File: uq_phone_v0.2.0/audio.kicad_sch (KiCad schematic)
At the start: 31 parts, among them J1 PJ-605-6A, U13 TS3A5018RSVR, U14 NAU88C22YG, U9 AZV5001RA4-7

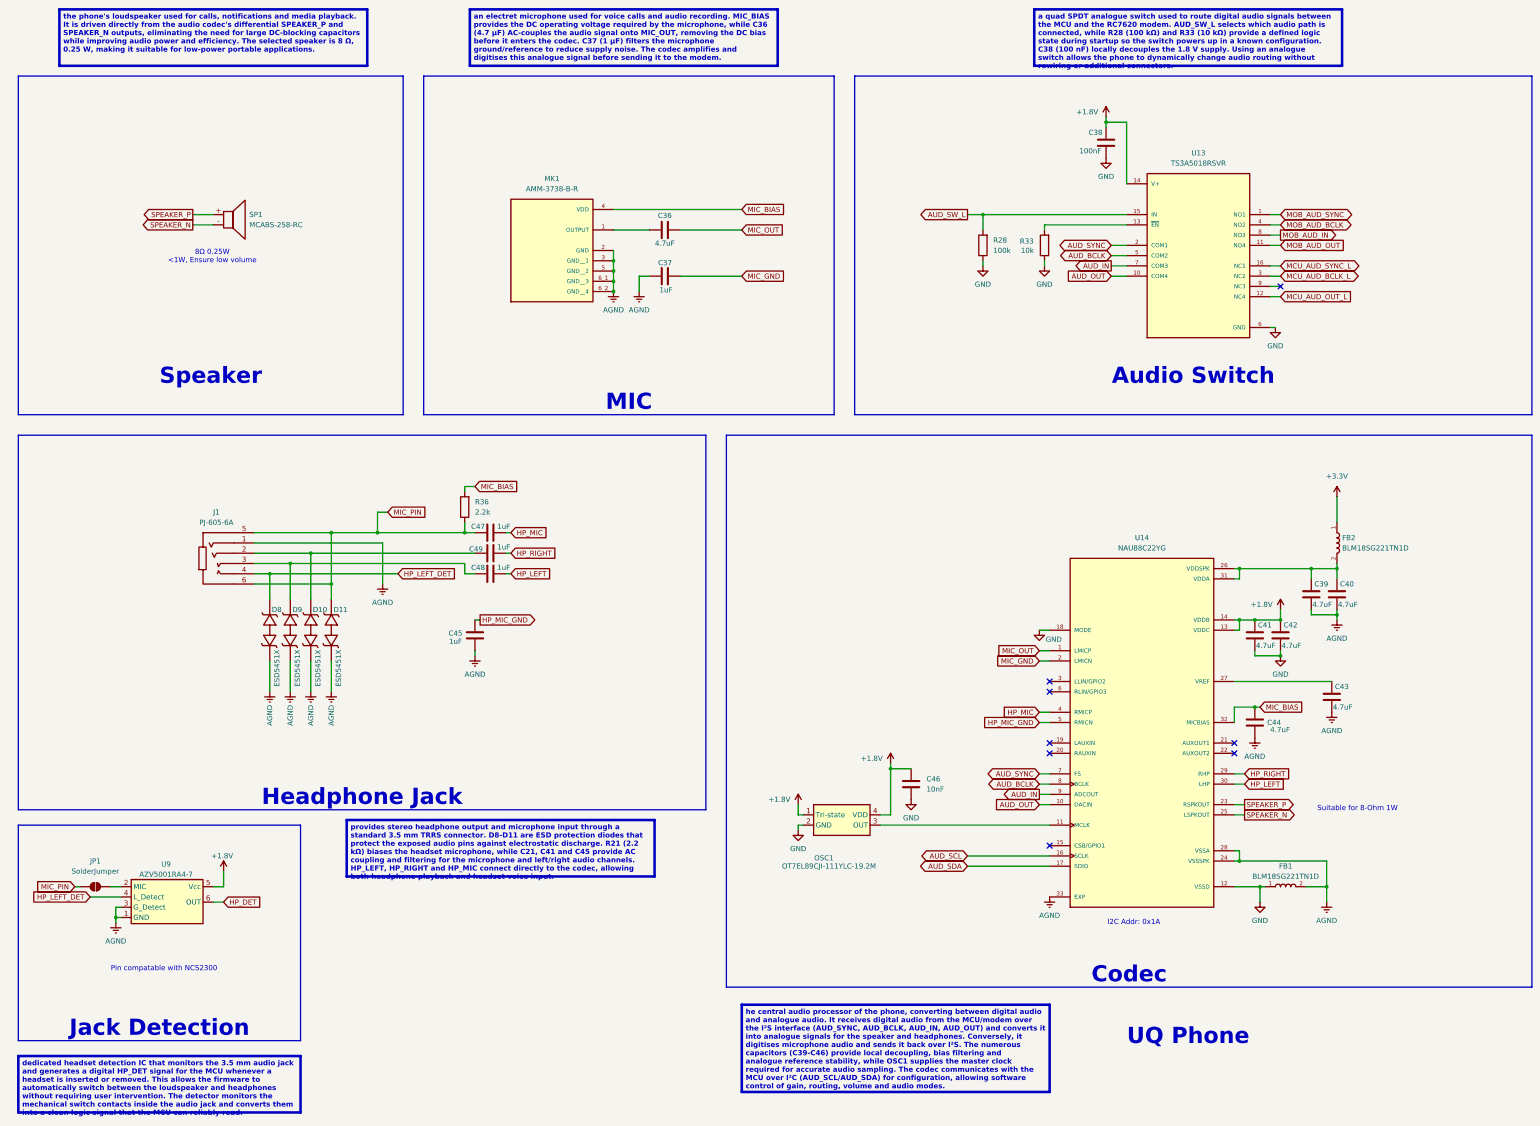
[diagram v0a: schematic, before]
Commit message: Add headphone breakout board and update main PCB
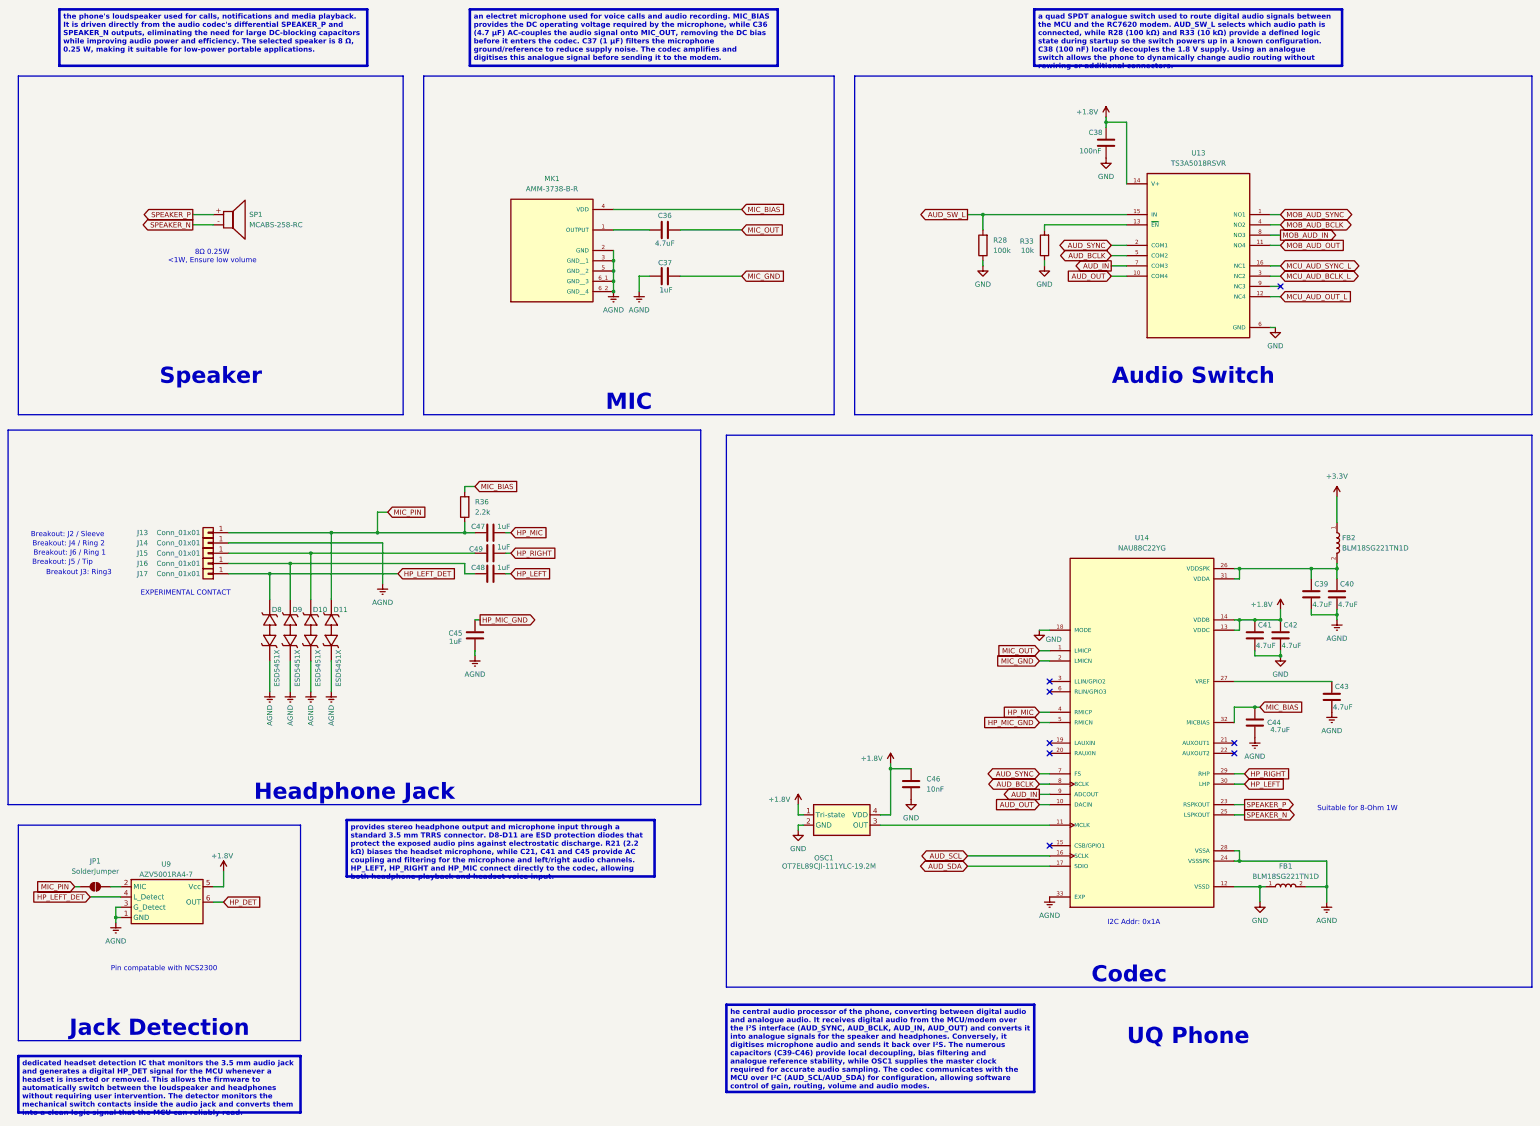
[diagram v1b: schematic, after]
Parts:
- removed J1: PJ-605-6A, custom_footprints:AUDIO-TH_PJ-605-6A, symbol Misc:PJ-605-6A
- added J13, J14, J15, J16, J17: Conn_01x01, headphone_board:Breakout_Mating_Pad, symbol Connector_Generic:Conn_01x01
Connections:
- net AGND: now also J14.1 (Pin_1)
- net HP_LEFT_DET: now also J17.1 (Pin_1)
- net MIC_PIN: now also J13.1 (Pin_1)
- net at C48.2, D9.2: now also J16.1 (Pin_1)
- net at C49.2, D10.2: now also J15.1 (Pin_1)
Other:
- note added: "Breakout J3: Ring3"
- note added: "Breakout: J2 / Sleeve"
- note added: "Breakout: J4 / Ring 2"
- note added: "Breakout: J5 / Tip"
- note added: "Breakout: J6 / Ring 1"
- note added: "EXPERIMENTAL CONTACT"

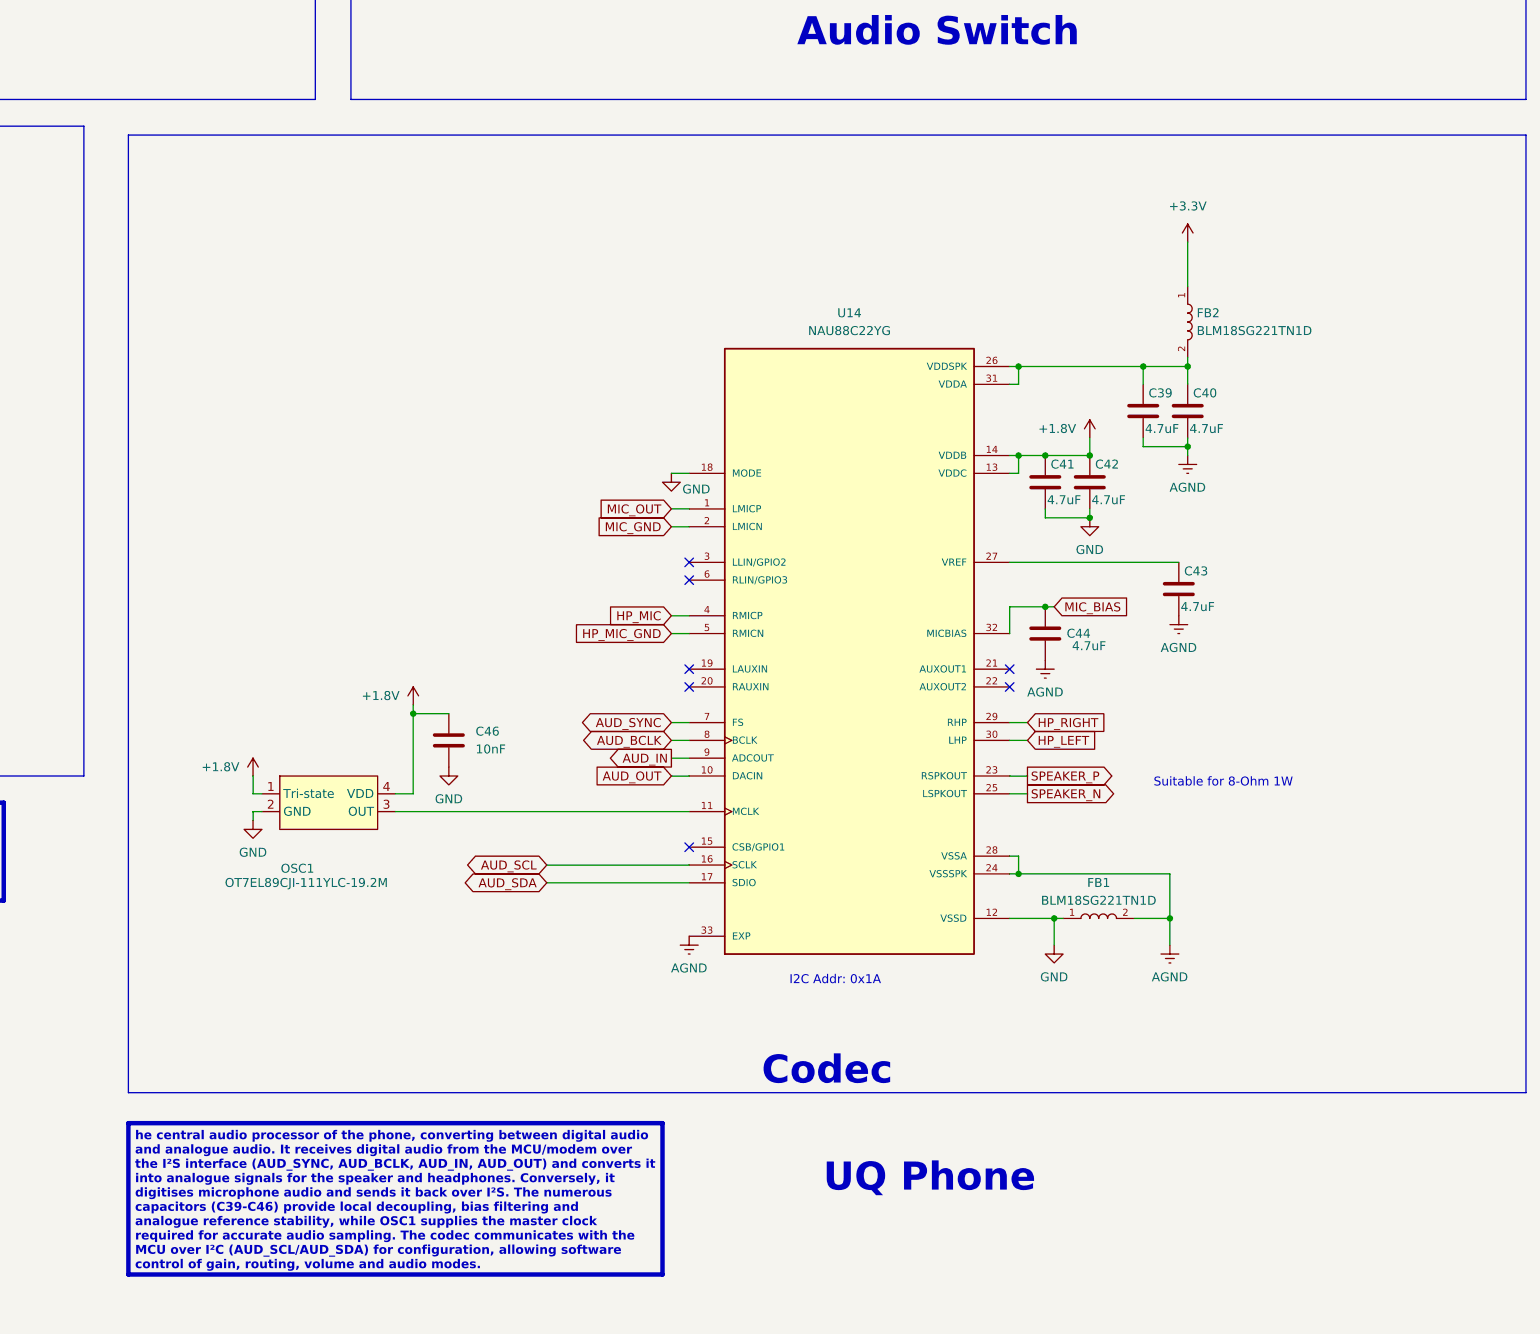
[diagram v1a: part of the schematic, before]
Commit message: Complete STM32H723ZGI6 144-pin schematic and FMC mapping
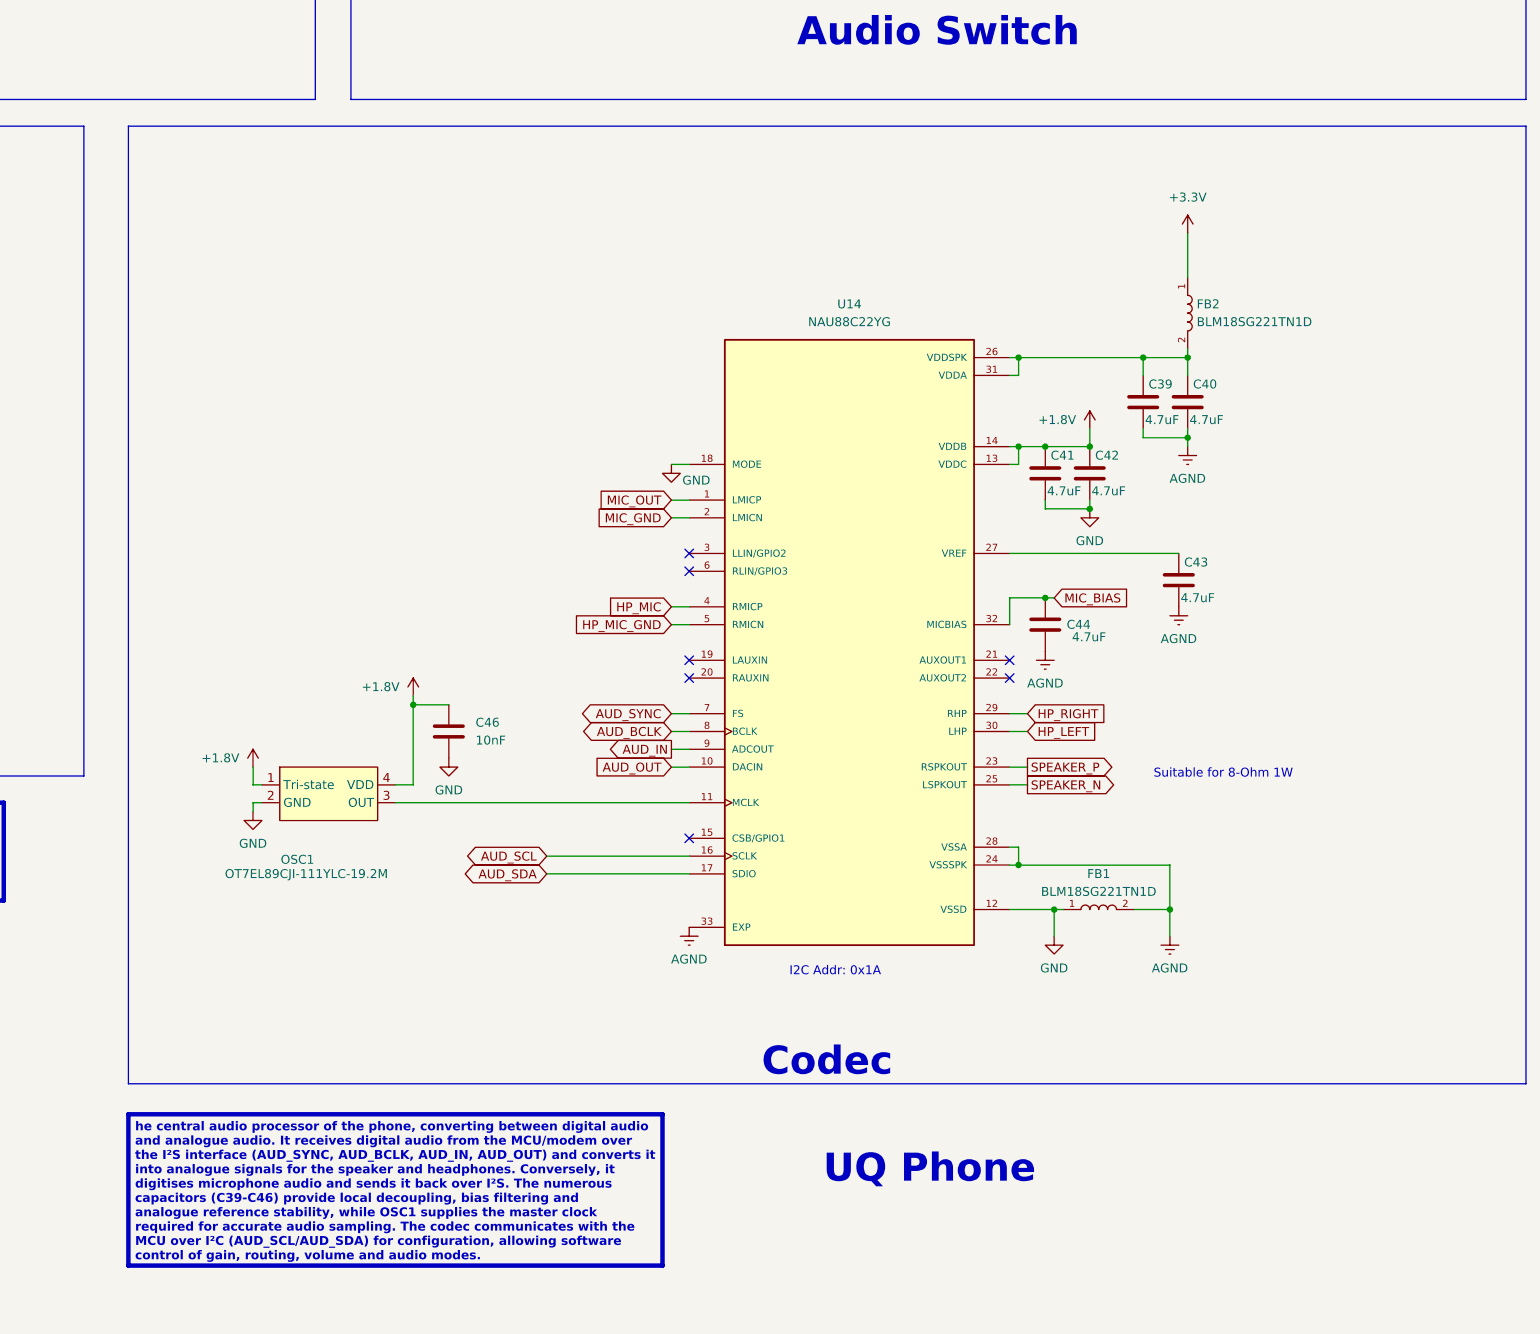
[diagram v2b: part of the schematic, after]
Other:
- moved on the sheet: C39, C40, C41, C42, C43, C44, C46, FB1, FB2, OSC1, U14

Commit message: Revert "Complete STM32H723ZGI6 144-pin schematic and FMC mapping"
This reverts commit c988dda79df5cbf87dce3ceded82a655262fe630.
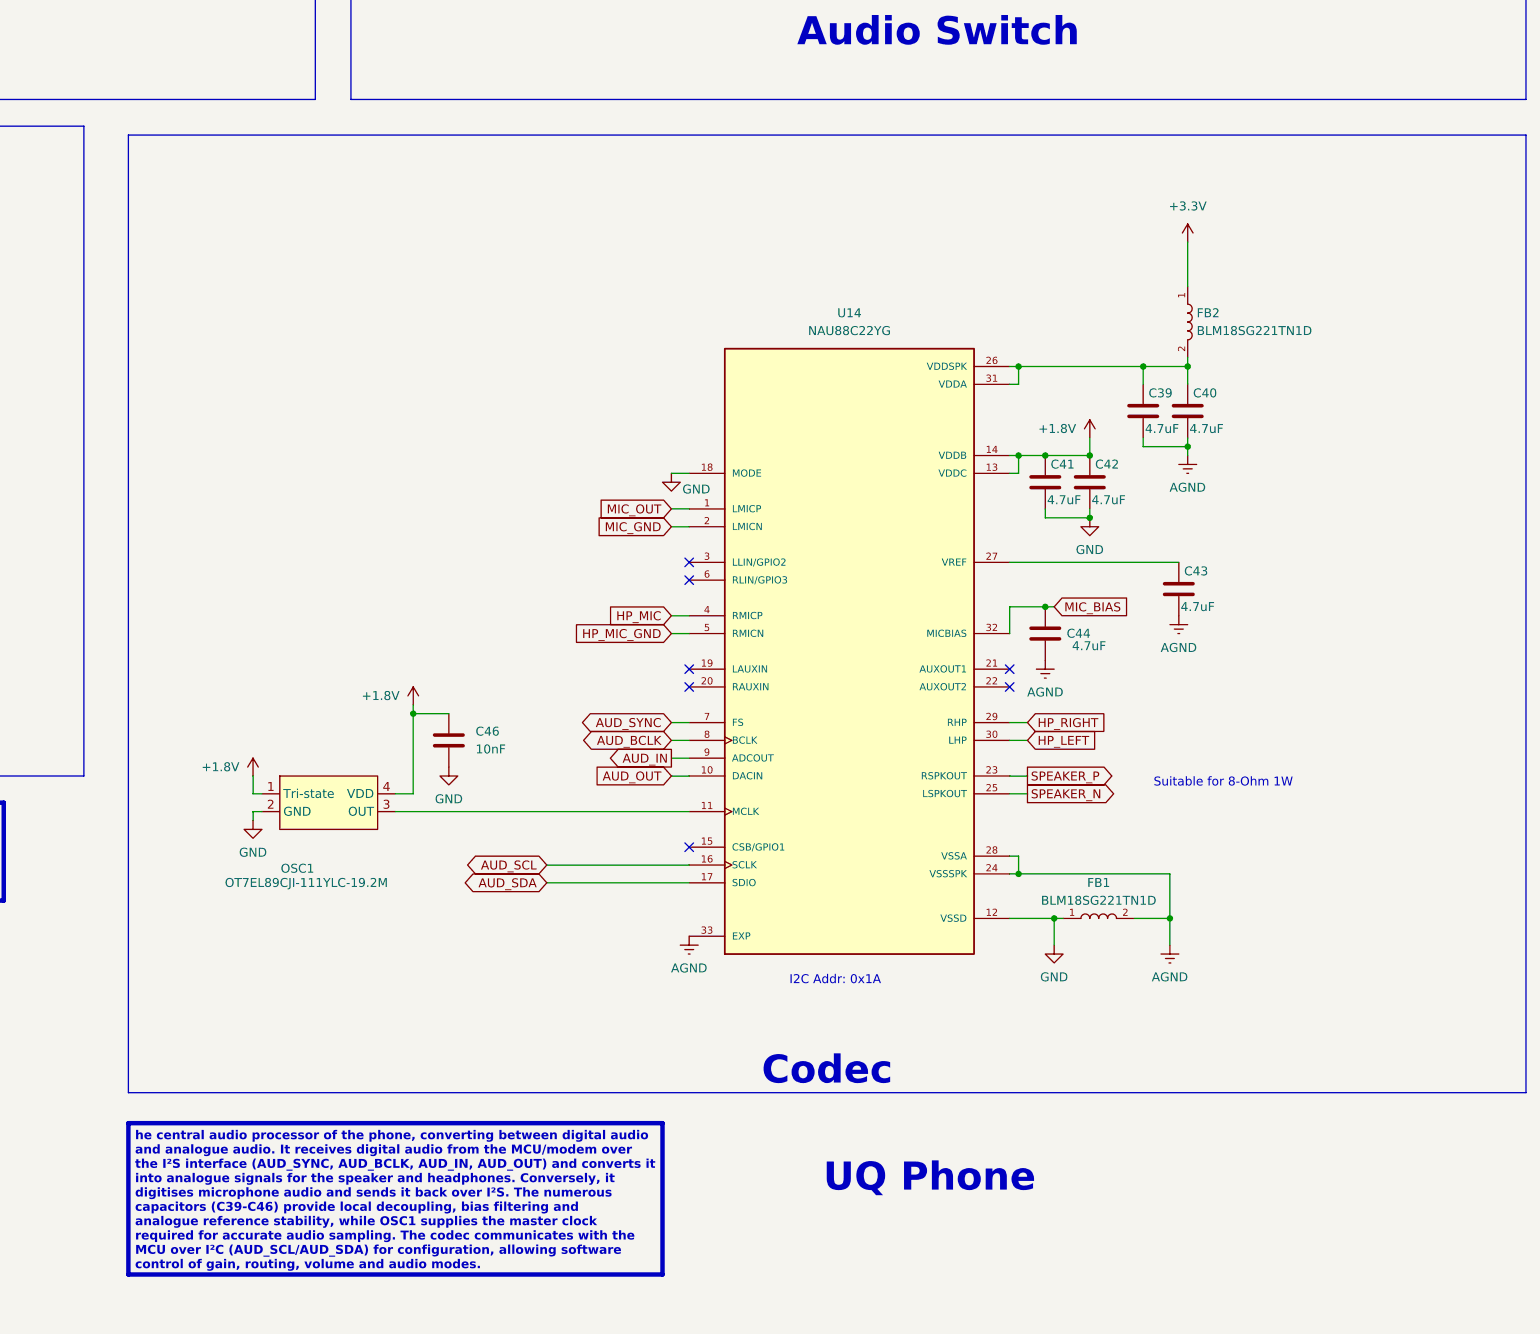
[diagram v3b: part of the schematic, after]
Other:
- moved on the sheet: C39, C40, C41, C42, C43, C44, C46, FB1, FB2, OSC1, U14
